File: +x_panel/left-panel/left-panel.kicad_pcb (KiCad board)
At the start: 2 copper layers, 85 x 270 mm, 14 parts

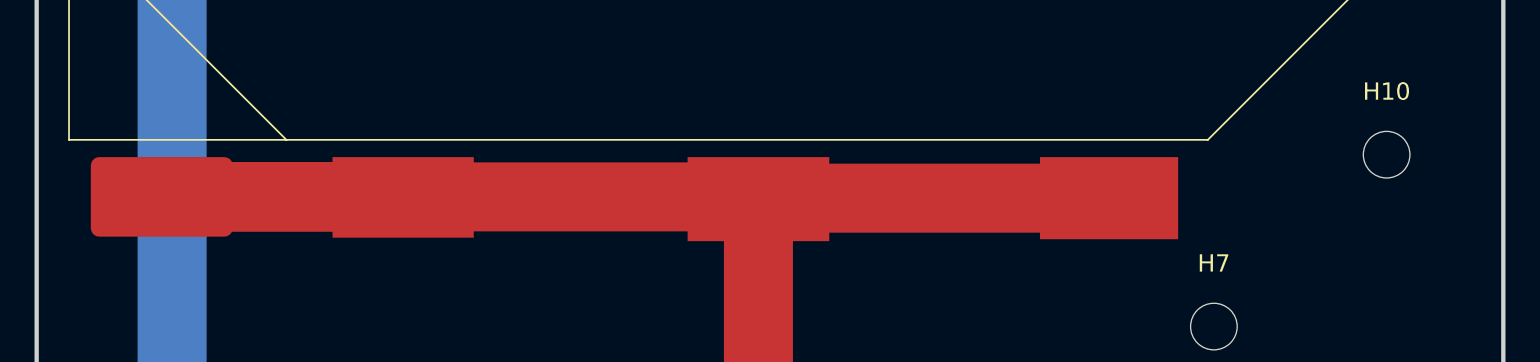
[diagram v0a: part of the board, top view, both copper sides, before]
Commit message: Updated panels based on dxf drawings from mech, need to move all holes up 5mm
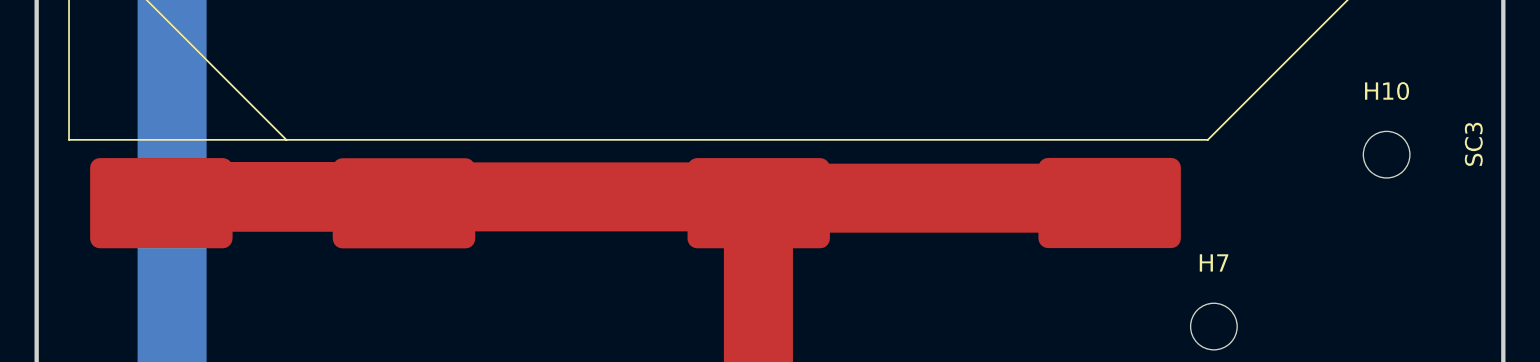
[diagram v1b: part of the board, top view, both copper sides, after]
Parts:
- SC3: footprint Solar_cell:Solar_Cell_Lightricity_S8040_CIC -> Solar_cell:Solar_Cell_Lightricity_S8040_CIC_Shorter_Tabs
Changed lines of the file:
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@@
 		)
 	)
-	(footprint "Solar_cell:Solar_Cell_Lightricity_S8040_CIC"
+	(footprint "Solar_cell:Solar_Cell_Lightricity_S8040_CIC_Shorter_Tabs"
 		(layer "F.Cu")
 		(at 835.825 227.535 90)
 		(property "Reference" "SC3"
-			(at 0.05 1.535 90)
+			(at -0.25 1.45 90)
 			(unlocked yes)
 			(layer "F.SilkS")
-			(hide yes)
 			(effects
 				(font
@@
 			)
 		)
-		(pad "1" smd rect
-			(at -3.435 -40.045 90)
-			(size 4.87 8.21)
+		(dimension
+			(type orthogonal)
+			(layer "Dwgs.User")
+			(pts
+				(xy 755.825 187.535) (xy 835.825 187.535)
+			)
+			(height -20.29)
+			(orientation 0)
+			(format
+				(prefix "")
+				(suffix "")
+				(units 3)
+				(units_format 0)
+				(precision 4)
+				(suppress_zeroes yes)
+			)
+			(style
+				(thickness 0.1)
+				(arrow_length 1.27)
+				(text_position_mode 0)
+				(arrow_direction outward)
+				(extension_height 0.58642)
+				(extension_offset 0.5)
+				(keep_text_aligned yes)
+			)
+			(gr_text "80"
+				(at 795.825 166.095 0)
+				(layer "Dwgs.User")
+				(effects
+					(font
+						(size 1 1)
+						(thickness 0.15)
+					)
+				)
+			)
+		)
+		(dimension
+			(type orthogonal)
+			(layer "Dwgs.User")
+			(pts
+				(xy 755.825 227.535) (xy 835.825 227.535)
+			)
+			(height 19.64)
+			(orientation 0)
+			(format
+				(prefix "")
+				(suffix "")
+				(units 3)
+				(units_format 0)
+				(precision 4)
+				(suppress_zeroes yes)
+			)
+			(style
+				(thickness 0.1)
+				(arrow_length 1.27)
+				(text_position_mode 0)
+				(arrow_direction outward)
+				(extension_height 0.58642)
+				(extension_offset 0.5)
+				(keep_text_aligned yes)
+			)
+			(gr_text "80"
+				(at 795.825 246.025 0)
+				(layer "Dwgs.User")
+				(effects
+					(font
+						(size 1 1)
+						(thickness 0.15)
+					)
+				)
+			)
+		)
+		(dimension
+			(type orthogonal)
+			(layer "Dwgs.User")
+			(pts
+				(xy 821.825 227.535) (xy 755.825 227.535)
+			)
+			(height 27.71)
+			(orientation 0)
+			(format
+				(prefix "")
+				(suffix "")
+				(units 3)
+				(units_format 0)
+				(precision 4)
+				(suppress_zeroes yes)
+			)
+			(style
+				(thickness 0.1)
+				(arrow_length 1.27)
+				(text_position_mode 0)
+				(arrow_direction outward)
+				(extension_height 0.58642)
+				(extension_offset 0.5)
+				(keep_text_aligned yes)
+			)
+			(gr_text "66"
+				(at 788.825 254.095 0)
+				(layer "Dwgs.User")
+				(effects
+					(font
+						(size 1 1)
+						(thickness 0.15)
+					)
+				)
+			)
+		)
+		(pad "1" smd roundrect
+			(at -3.6775 -60.58625 270)
+			(size 5.225 8.2525)
 			(layers "F.Cu" "F.Mask" "F.Paste")
+			(roundrect_rratio 0.1067235859)
 			(net 3 "Net-(SC1--)")
 			(pinfunction "+")
 			(pintype "passive")
-			(thermal_bridge_angle 45)
-		)
-		(pad "1" smd rect
-			(at -3.38 -19.725 90)
-			(size 4.76 8.01)
+		)
+		(pad "1" smd roundrect
+			(at -3.67 -74.65 270)
+			(size 5.225 8.2525)
 			(layers "F.Cu" "F.Mask" "F.Paste")
+			(roundrect_rratio 0.1067235859)
 			(net 3 "Net-(SC1--)")
 			(pinfunction "+")
 			(pintype "passive")
-			(thermal_bridge_angle 45)
-		)
-		(pad "1" smd rect
-			(at -3.335 -60.635 90)
-			(size 4.67 8.19)
+		)
+		(pad "1" smd roundrect
+			(at -3.67 -40.03 270)
+			(size 5.225 8.2525)
 			(layers "F.Cu" "F.Mask" "F.Paste")
+			(roundrect_rratio 0.1067235859)
 			(net 3 "Net-(SC1--)")
 			(pinfunction "+")
 			(pintype "passive")
-			(thermal_bridge_angle 45)
 		)
 		(pad "1" smd roundrect
-			(at -3.305 -74.6225 90)
-			(size 4.61 8.225)
+			(at -3.66 -19.69 270)
+			(size 5.225 8.2525)
 			(layers "F.Cu" "F.Mask" "F.Paste")
 			(roundrect_rratio 0.1067235859)

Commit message: moved holes up 5mm, did what Jack said to do
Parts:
- Buck1: footprint Connection_Pads:2_Hirose_Pin -> Connection_Pads:DF13_Horizontal
- SC3: footprint Solar_cell:Solar_Cell_Lightricity_S8040_CIC_Shorter_Tabs -> Solar_cell:Solar_Cell_Lightricity_S8040_CIC
- moved Buck1 8.76 mm to (820.2, 62.5)
- moved SC3 1.62 mm to (836.1, 225.9)
- moved SC4 1.34 mm to (836.1, 184.8)
- moved SC5 0.76 mm to (836.1, 143.8)
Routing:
- net Net-(Buck1-BCR+): track 336.4 -> 247.8 mm
- net Net-(SC4--): track 55.0 -> 75.4 mm
- net Net-(Buck1-BCR-): track 43.5 -> 23.9 mm, vias 1 -> 0
- net Net-(SC3--): track 72.7 -> 75.6 mm
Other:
- outline, holes or cut-outs redrawn

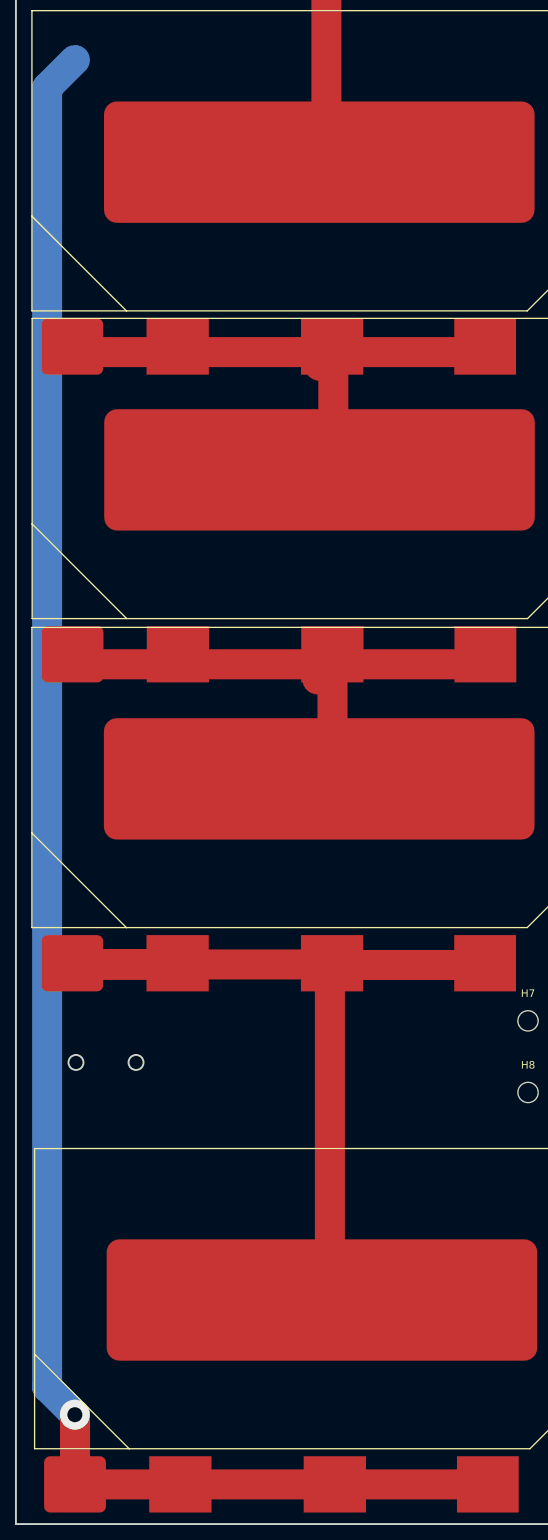
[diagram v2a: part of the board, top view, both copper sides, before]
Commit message: Moved some things around, locked some components
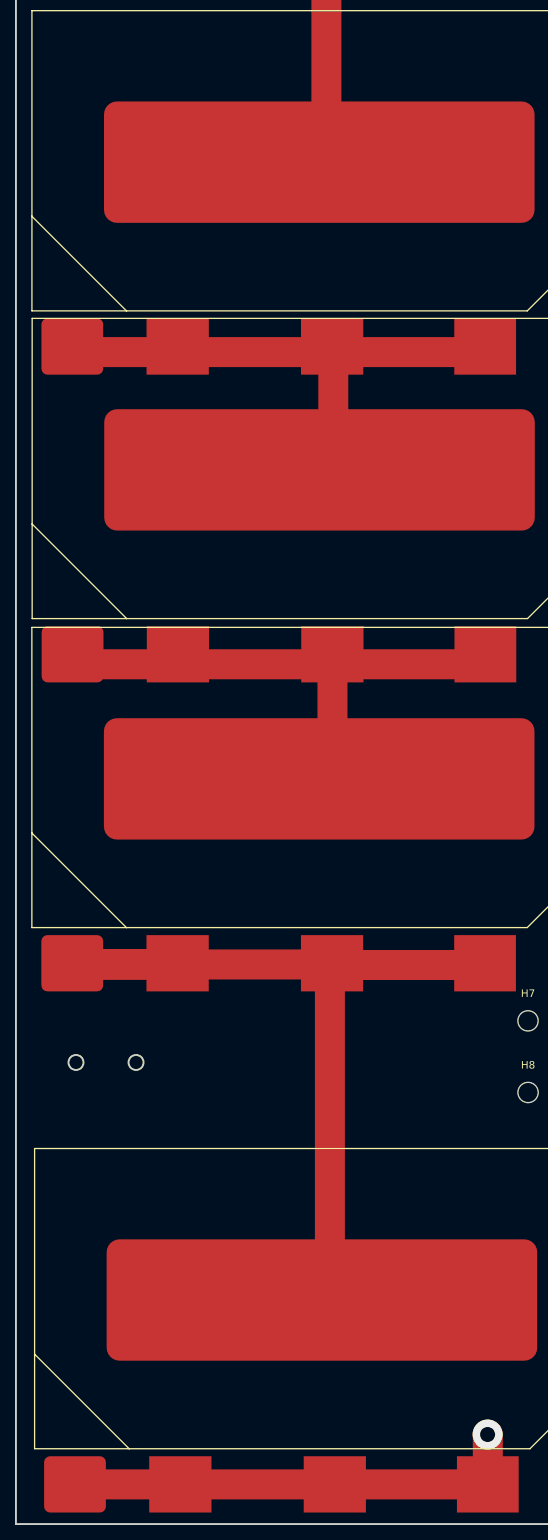
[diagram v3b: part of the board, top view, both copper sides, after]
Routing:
- net Net-(Buck1-BCR+): track 247.8 -> 61.7 mm
- net Net-(SC3--): track 75.6 -> 72.7 mm
- net Net-(SC4--): track 75.4 -> 72.8 mm
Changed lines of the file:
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@@
+	)
+	(segment
+		(start 816.82 300.115)
+		(end 816.82 293.5)
+		(width 4)
+		(layer "F.Cu")
+		(net 2)
 	)
 	(segment
 		(start 761.8175 300.115)
 		(end 775.855 300.115)
+		(width 4)
+		(layer "F.Cu")
+		(net 2)
+	)
+	(segment
+		(start 761.8175 300.0975)
+		(end 761.8175 300.115)
 		(width 4)
 		(layer "F.Cu")
@@
 	)
 	(segment
+		(start 816.82 293.5)
+		(end 816.79 293.47)
+		(width 4)
+		(layer "F.Cu")
+		(net 2)
+	)
+	(segment
 		(start 816.82 300.115)
 		(end 796.435 300.115)
@@
 		(net 2)
 	)
-	(segment
-		(start 761.8175 290.8475)
-		(end 761.8 290.83)
-		(width 4)
-		(layer "F.Cu")
-		(net 2)
-	)
-	(segment
-		(start 761.8175 300.115)
-		(end 761.8175 290.8475)
-		(width 4)
-		(layer "F.Cu")
-		(net 2)
-	)
 	(via
-		(at 761.8 290.83)
+		(at 816.79 293.47)
 		(size 4)
 		(drill 2)
 		(layers "F.Cu" "B.Cu")
-		(net 2)
-	)
-	(segment
-		(start 761.8 290.83)
-		(end 758.1 287.13)
-		(width 4)
-		(layer "B.Cu")
-		(net 2)
-	)
-	(segment
-		(start 758.1 114.04)
-		(end 761.8 110.34)
-		(width 4)
-		(layer "B.Cu")
-		(net 2)
-	)
-	(segment
-		(start 758.1 287.13)
-		(end 758.1 114.04)
-		(width 4)
-		(layer "B.Cu")
 		(net 2)
 	)
@@
 	)
 	(segment
-		(start 794.11 192.86)
-		(end 796.125 190.845)
-		(width 4)
-		(layer "F.Cu")
-		(net 4)
-	)
-	(segment
 		(start 796.125 205.705)
 		(end 794.11 207.72)
@@
 		(width 4)
 		(layer "F.Cu")
-		(net 5)
-	)
-	(segment
-		(start 794.41 151.08)
-		(end 796.235 149.255)
-		(width 4)
-		(layer "F.Cu")

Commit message: changed ALOT of things, got it to a point to send mech models,solar panel harness on BS need changed
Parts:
- SC3: footprint Solar_cell:Solar_Cell_Lightricity_S8040_CIC -> Solar_cell:Solar_Cell_Lightricity_S8040_CIC_Shorter_Tabs
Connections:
- SC1 pad 1: Net-(Buck1-BCR+) -> Net-(Buck1-BCR-)
- SC6 pad 2: Net-(Buck1-BCR-) -> Net-(Buck1-BCR+)
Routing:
- net Net-(Buck1-BCR-): track 23.9 -> 292.1 mm, vias 0 -> 1
- net Net-(Buck1-BCR+): track 61.7 -> 65.2 mm
- added copper zone on B.Cu, net Net-(Buck1-BCR+)
- added copper zone on B.Cu, net Net-(Buck1-BCR-)
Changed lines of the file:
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@@
 	(net 6 "Net-(SC5--)")
 	(footprint "MountingHole:MountingHole_2.7mm"
+		(locked yes)
 		(layer "F.Cu")
 		(at 832.193925 99.904828)
@@
 	)
 	(footprint "MountingHole:MountingHole_2.7mm"
+		(locked yes)
 		(layer "F.Cu")
 		(at 822.175863 99.889019)
@@
 	)
 	(footprint "MountingHole:MountingHole_2.7mm"
+		(locked yes)
 		(layer "F.Cu")
 		(at 822.186445 90.344174)
@@
 	)
 	(footprint "MountingHole:MountingHole_2.7mm"
+		(locked yes)
 		(layer "F.Cu")
 		(at 832.225982 247.87505)
@@
 	)
 	(footprint "MountingHole:MountingHole_2.7mm"
+		(locked yes)
 		(layer "F.Cu")
 		(at 822.182238 247.899219)
@@
 	)
 	(footprint "Solar_cell:Solar_Cell_Lightricity_S8040_CIC"
+		(locked yes)
 		(layer "F.Cu")
 		(at 836.11 184.76 90)
@@
 		)
 	)
-	(footprint "Solar_cell:Solar_Cell_Lightricity_S8040_CIC"
+	(footprint "Solar_cell:Solar_Cell_Lightricity_S8040_CIC_Shorter_Tabs"
+		(locked yes)
 		(layer "F.Cu")
 		(at 836.07 225.93 90)
@@
 			)
 		)
-		(property "Datasheet" ""
+		(property "Datasheet" "~"
 			(at -0.25 1.95 90)
 			(unlocked yes)
@@
 			)
 		)
-		(property "Description" ""
+		(property "Description" "Single solar cell"
 			(at -0.25 1.95 90)
 			(unlocked yes)
@@
 			(layer "Dwgs.User")
 			(pts
-				(xy 756.07 185.93) (xy 836.07 185.93)
+				(xy 756.07 225.93) (xy 836.07 225.93)
 			)
-			(height -20.29)
+			(height 19.64)
 			(orientation 0)
 			(format
@@
 			)
 			(gr_text "80"
-				(at 796.07 164.49 0)
+				(at 796.07 244.42 0)
 				(layer "Dwgs.User")
 				(effects
@@
 			(layer "Dwgs.User")
 			(pts
-				(xy 756.07 225.93) (xy 836.07 225.93)
+				(xy 756.07 185.93) (xy 836.07 185.93)
 			)
-			(height 19.64)
+			(height -20.29)
 			(orientation 0)
 			(format
@@
 			)
 			(gr_text "80"
-				(at 796.07 244.42 0)
+				(at 796.07 164.49 0)
 				(layer "Dwgs.User")
 				(effects
@@
 		)
 		(pad "1" smd roundrect
-			(at -4.75 -74.6175 90)
-			(size 7.5 8.235)
+			(at -3.6775 -60.58625 270)
+			(size 5.225 8.2525)
 			(layers "F.Cu" "F.Mask" "F.Paste")
 			(roundrect_rratio 0.1067235859)
@@
 			(pintype "passive")
 		)
-		(pad "1" smd rect
-			(at -4.75 -60.58 90)
-			(size 7.5 8.3)
+		(pad "1" smd roundrect
+			(at -3.67 -74.65 270)
+			(size 5.225 8.2525)
 			(layers "F.Cu" "F.Mask" "F.Paste")
+			(roundrect_rratio 0.1067235859)
 			(net 3 "Net-(SC1--)")
 			(pinfunction "+")
 			(pintype "passive")
-			(thermal_bridge_angle 45)
 		)
-		(pad "1" smd rect
-			(at -4.75 -40 90)
-			(size 7.5 8.3)
+		(pad "1" smd roundrect
+			(at -3.67 -40.03 270)
+			(size 5.225 8.2525)
 			(layers "F.Cu" "F.Mask" "F.Paste")
+			(roundrect_rratio 0.1067235859)
 			(net 3 "Net-(SC1--)")
 			(pinfunction "+")
 			(pintype "passive")
-			(thermal_bridge_angle 45)
 		)
-		(pad "1" smd rect
-			(at -4.75 -19.615 90)
-			(size 7.5 8.23)
+		(pad "1" smd roundrect
+			(at -3.66 -19.69 270)
+			(size 5.225 8.2525)
 			(layers "F.Cu" "F.Mask" "F.Paste")
+			(roundrect_rratio 0.1067235859)
 			(net 3 "Net-(SC1--)")
 			(pinfunction "+")
 			(pintype "passive")
-			(thermal_bridge_angle 45)
 		)
 		(pad "2" smd roundrect
@@
 	)
 	(footprint "MountingHole:MountingHole_2.7mm"
+		(locked yes)
 		(layer "F.Cu")
 		(at 832.1926 80.382494 90)
@@
 	)
 	(footprint "Solar_cell:Solar_Cell_Lightricity_S8040_CIC"
+		(locked yes)
 		(layer "F.Cu")
 		(at 836.435 295.365 90)
@@
 			(layers "F.Cu" "F.Mask" "F.Paste")
 			(roundrect_rratio 0.1067235859)
-			(net 2 "Net-(Buck1-BCR+)")
+			(net 1 "Net-(Buck1-BCR-)")
 			(pinfunction "+")
 			(pintype "passive")
@@
 			(size 7.5 8.3)
 			(layers "F.Cu" "F.Mask" "F.Paste")
-			(net 2 "Net-(Buck1-BCR+)")
+			(net 1 "Net-(Buck1-BCR-)")
 			(pinfunction "+")
 			(pintype "passive")
@@
 			(size 7.5 8.3)
 			(layers "F.Cu" "F.Mask" "F.Paste")
-			(net 2 "Net-(Buck1-BCR+)")
+			(net 1 "Net-(Buck1-BCR-)")
 			(pinfunction "+")
 			(pintype "passive")
@@
 			(size 7.5 8.23)
 			(layers "F.Cu" "F.Mask" "F.Paste")
-			(net 2 "Net-(Buck1-BCR+)")
+			(net 1 "Net-(Buck1-BCR-)")
 			(pinfunction "+")
 			(pintype "passive")
@@
 	)
 	(footprint "Solar_cell:Solar_Cell_Lightricity_S8040_CIC"
+		(locked yes)
 		(layer "F.Cu")
 		(at 836.08 143.76 90)
@@
 	)
 	(footprint "Solar_cell:Solar_Cell_Lightricity_S8040_CIC"
+		(locked yes)
 		(layer "F.Cu")
 		(at 835.315 78.47 90)
@@
 			(layers "F.Cu" "F.Mask" "F.Paste")
 			(roundrect_rratio 0.1067235859)
-			(net 1 "Net-(Buck1-BCR-)")
+			(net 2 "Net-(Buck1-BCR+)")
 			(pinfunction "-")
 			(pintype "passive")
@@
 	)
 	(footprint "MountingHole:MountingHole_2.7mm"
+		(locked yes)
 		(layer "F.Cu")
 		(at 822.175686 238.355633)
@@
 	)
 	(footprint "MountingHole:MountingHole_2.7mm"
+		(locked yes)
 		(layer "F.Cu")
 		(at 832.187269 228.39481)
@@
 	)
 	(footprint "Connection_Pads:DF13_Horizontal"
+		(locked yes)
 		(layer "B.Cu")
 		(at 820.183274 62.54 -90)
@@
 		)
 		(fill no)
+		(locked yes)
 		(layer "Edge.Cuts")
 	)
@@
 		)
 		(fill no)
+		(locked yes)
 		(layer "Edge.Cuts")
 	)
@@
 		)
 		(fill no)
+		(locked yes)
 		(layer "Edge.Cuts")
 	)
@@
 		)
 		(fill no)
+		(locked yes)
 		(layer "Edge.Cuts")
 	)
@@
 	)
 	(segment
-		(start 793.6 58.655)
-		(end 817.505 58.655)
-		(width 4)
-		(layer "F.Cu")
-		(net 1)
-	)
-	(segment
 		(start 816.82 300.115)
 		(end 816.82 293.5)
 		(width 4)
 		(layer "F.Cu")
-		(net 2)
+		(net 1)
 	)
 	(segment
@@
 		(width 4)
 		(layer "F.Cu")
-		(net 2)
+		(net 1)
 	)
 	(segment
@@
 		(width 4)
 		(layer "F.Cu")
-		(net 2)
+		(net 1)
 	)
 	(segment
@@
 		(width 4)
 		(layer "F.Cu")
-		(net 2)
+		(net 1)
 	)
 	(segment
@@
 		(width 4)
 		(layer "F.Cu")
-		(net 2)
+		(net 1)
 	)
 	(segment
@@
 		(width 4)
 		(layer "F.Cu")
-		(net 2)
+		(net 1)
 	)
 	(via
@@
 		(drill 2)
 		(layers "F.Cu" "B.Cu")
+		(net 1)
+	)
+	(segment
+		(start 817.595 63.955)
+		(end 818.208274 63.955)
+		(width 3)
+		(layer "B.Cu")
+		(net 1)
+	)
+	(segment
+		(start 816.79 64.76)
+		(end 817.595 63.955)
+		(width 3)
+		(layer "B.Cu")
+		(net 1)
+	)
+	(segment
+		(start 816.79 65.48)
+		(end 816.79 64.76)
+		(width 3)
+		(layer "B.Cu")
+		(net 1)
+	)
+	(segment
+		(start 816.79 293.47)
+		(end 816.79 65.48)
+		(width 4)
+		(layer "B.Cu")
+		(net 1)
+	)
+	(segment
+		(start 816.13742 58.655)
+		(end 793.6 58.655)
+		(width 4)
+		(layer "F.Cu")
+		(net 2)
+	)
+	(segment
+		(start 817.7 59.6)
+		(end 817.08242 59.6)
+		(width 4)
+		(layer "F.Cu")
+		(net 2)
+	)
+	(segment
+		(start 817.08242 59.6)
+		(end 816.13742 58.655)
+		(width 4)
+		(layer "F.Cu")
+		(net 2)
+	)
+	(segment
+		(start 807.525 58.655)
+		(end 793.6 58.655)
+		(width 3)
+		(layer "F.Cu")
+		(net 2)
+	)
+	(segment
+		(start 817.57 48.61)
+		(end 807.525 58.655)
+		(width 3)
+		(layer "F.Cu")
+		(net 2)
+	)
+	(via
+		(at 817.57 48.61)
+		(size 4)
+		(drill 2)
+		(layers "F.Cu" "B.Cu")
+		(net 2)
+	)
+	(segment
+		(start 817.934 60.754)
+		(end 818.208274 60.754)
+		(width 3)
+		(layer "B.Cu")
+		(net 2)
+	)
+	(segment
+		(start 817.57 48.61)
+		(end 817.57 60.39)
+		(width 3)
+		(layer "B.Cu")
+		(net 2)
+	)
+	(segment
+		(start 817.57 60.39)
+		(end 817.934 60.754)
+		(width 3)
+		(layer "B.Cu")
 		(net 2)
 	)
@@
 		(net 6)
 	)
+	(zone
+		(net 2)
+		(net_name "Net-(Buck1-BCR+)")
+		(layer "B.Cu")
+		(hatch edge 0.5)
+		(priority 1)
+		(connect_pads
+			(clearance 0)
+		)
+		(min_thickness 0.25)
+		(filled_areas_thickness no)
+		(fill yes
+			(thermal_gap 0.5)
+			(thermal_bridge_width 0.5)
+			(island_removal_mode 1)
+			(island_area_min 10)
+		)
+		(polygon
+			(pts
+				(xy 818.43 58.89) (xy 818.683685 61.86174) (xy 818.46 61.86) (xy 817.44 61.85) (xy 817.460757 61.86259)
+				(xy 816.713351 59.294888) (xy 818.95 59.05)
+			)
+		)
+	)
+	(zone
+		(net 1)
+		(net_name "Net-(Buck1-BCR-)")
+		(layer "B.Cu")
+		(hatch edge 0.5)
+		(connect_pads
+			(clearance 0)
+		)
+		(min_thickness 0.25)
+		(filled_areas_thickness no)
+		(fill yes
+			(thermal_gap 0.5)
+			(thermal_bridge_width 0.5)
+			(island_removal_mode 1)
+			(island_area_min 10)
+		)
+		(polygon
+			(pts
+				(xy 816.7 62.79) (xy 815.740318 65.518735) (xy 819.29 65.52) (xy 819.011399 62.678607)
+			)
+		)
+	)
 	(embedded_fonts no)
